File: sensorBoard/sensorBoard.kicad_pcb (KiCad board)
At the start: 4 copper layers, 204 x 100 mm, 162 parts, among them J10 Conn_01x07, J11 Conn_01x03, J12 Conn_01x02, J13 Conn_01x04, J14 Conn_01x05, J15 Conn_01x02, J16 Conn_01x02, J17 Conn_01x04, J18 Conn_01x07, J19 Conn_01x03, J20 Conn_01x02, J21 Conn_01x04, J22 Conn_01x05, J23 Conn_01x02, J24 Conn_01x02, J9 Conn_01x04, K5 G2RL-1-H, K6 G2RL-1-H, Q10 2N7002, Q11 2SC4213, Q12 NTD3055, Q19 2SC4213, Q2 2N7002, Q20 NTD3055, Q21 2N7002, Q22 2N7002, Q23 BSC440N10NS3G, Q24 BSC440N10NS3G, Q25 BSC440N10NS3G, Q26 BSC440N10NS3G, U12 MCP2551-I-SN, U17 LD1117S33TR_SOT223, U20 BTS50080-1TEA, U21 LM75C, U23 STM32L476RGTx, U32 BTS50080-1TEA, U33 LM75C, U35 STM32L476RGTx, U36 4011, U38 4011, U39 4011, U40 4011, U42 4N25, U43 4N25, U7 LD1117S33TR_SOT223, U9 MCP2551-I-SN, Y2 8MHz, Y3 8MHz

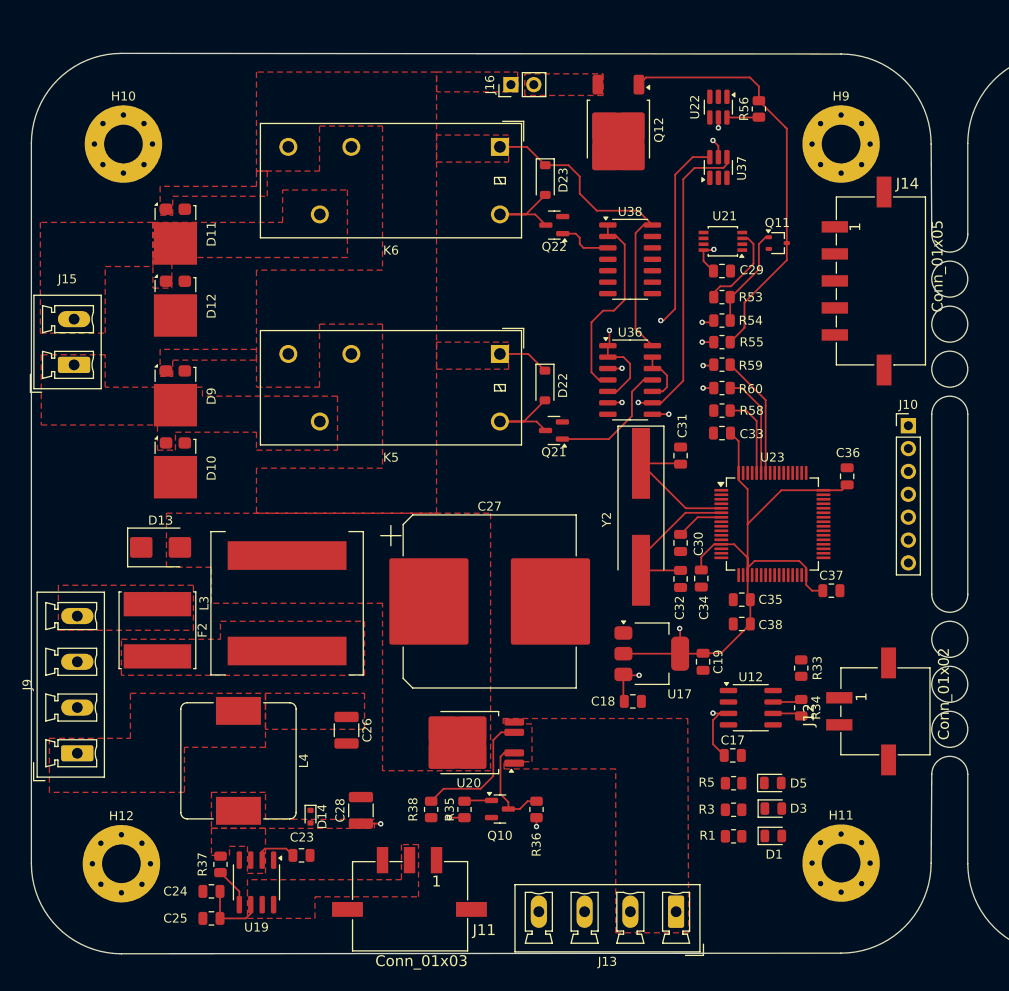
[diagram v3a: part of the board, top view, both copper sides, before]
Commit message: Das erstes PCB ist fast fertig. Die Vias waren auf die Platine platziert und Poligon war gefüllt.
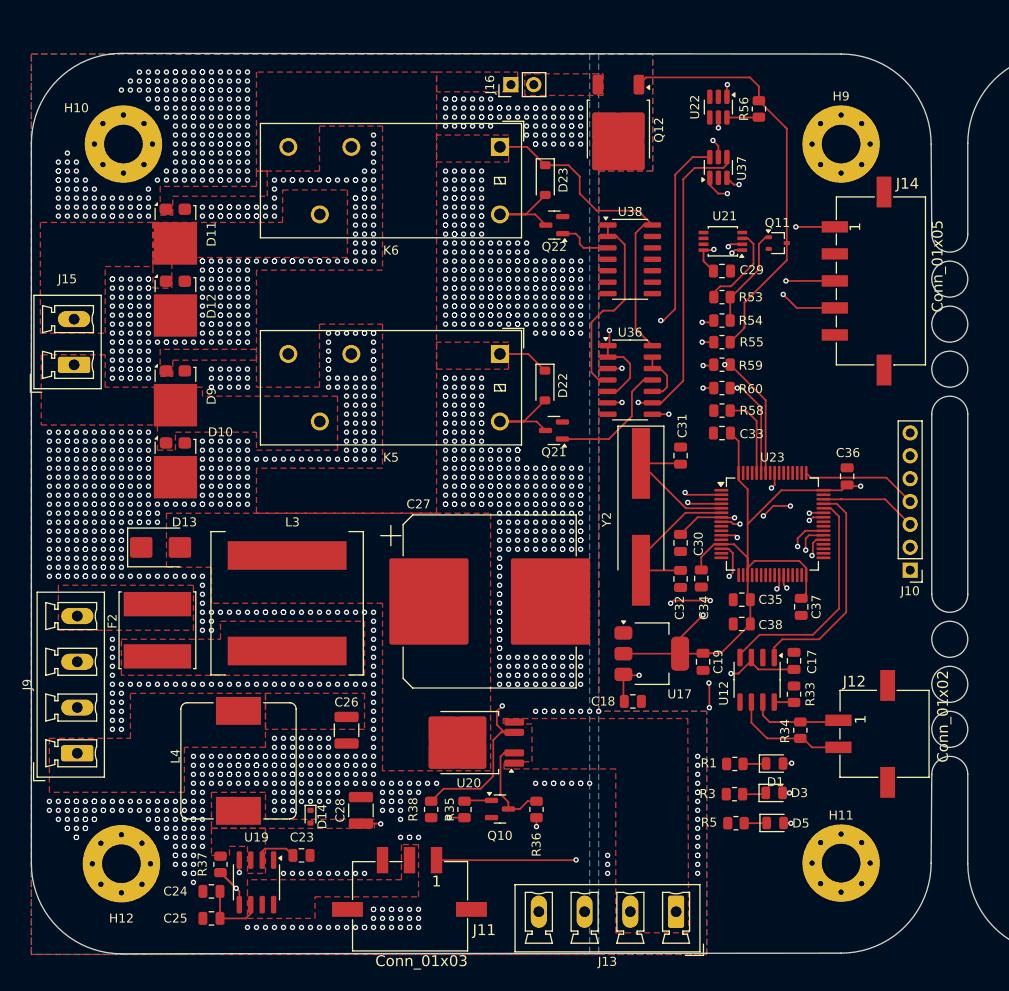
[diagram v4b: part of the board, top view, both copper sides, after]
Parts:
- moved J10 16.0 mm to (127.6, 97.3), turned to 180 degrees
- moved C17 12.5 mm to (114.7, 107.4), turned to 90 degrees
- moved D1 8.04 mm to (112.5, 118.8)
- moved R1 8.04 mm to (108.1, 118.8)
- moved D5 4.45 mm to (112.6, 125.4)
- moved R5 4.45 mm to (108.3, 125.4)
- moved C37 3.80 mm to (115.5, 101.4), turned to -90 degrees
- moved U12 3.18 mm to (110.6, 109.5), turned to -90 degrees
- moved R33 3.01 mm to (114.7, 111.1)
- moved J12 2.50 mm to (125.1, 115.5)
- moved R34 2.50 mm to (115.4, 115.1)
- moved R3 1.74 mm to (108.1, 122.2)
- moved D3 1.74 mm to (112.5, 122.1)
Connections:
- J10 pad 1: /Platine1/microcontroller1/UART_RX -> /Platine1/microcontroller1/UART_TX
- J10 pad 2: /Platine1/microcontroller1/UART_TX -> /Platine1/microcontroller1/UART_RX
- U23 pad 16: /Platine1/microcontroller1/UART_TX -> unconnected-(U23-PA2-Pad16)
- U23 pad 17: /Platine1/microcontroller1/UART_RX -> unconnected-(U23-PA3-Pad17)
- U23 pad 42: unconnected-(U23-PA9-Pad42) -> /Platine1/microcontroller1/UART_TX
- U23 pad 43: unconnected-(U23-PA10-Pad43) -> /Platine1/microcontroller1/UART_RX
- U35 pad 16: /Platine2/microcontroller2/UART_TX -> unconnected-(U35-PA2-Pad16)
- U35 pad 17: /Platine2/microcontroller2/UART_RX -> unconnected-(U35-PA3-Pad17)
- U35 pad 42: unconnected-(U35-PA9-Pad42) -> /Platine2/microcontroller2/UART_TX
- U35 pad 43: unconnected-(U35-PA10-Pad43) -> /Platine2/microcontroller2/UART_RX
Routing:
- net /Platine1/Commutation1-1/OVER_CURR_SERVO: track 4.43 -> 109.8 mm, vias 0 -> 2
- net /Platine1/Commutation1-1/SERVO_EN: track 0.00 -> 83.7 mm, vias 0 -> 4
- net /Platine1/SERVO_PWM: track 0.00 -> 59.8 mm, vias 0 -> 2
- net /Platine1/LED_EN: track 1.71 -> 58.9 mm, vias 1 -> 2
- net /Platine1/DIN: track 0.00 -> 56.5 mm, vias 0 -> 2
- net /Platine1/EN_MOTOR: track 0.00 -> 55.1 mm, vias 0 -> 2
- net /Platine1/TemperaturRegelung1/FAN_EN: track 0.00 -> 52.7 mm, vias 0 -> 2
- net /Platine1/IS_DIAG: track 14.7 -> 60.8 mm, vias 0 -> 4
- net Net-(D5-A): track 0.00 -> 34.3 mm, vias 0 -> 2
- net Net-(D3-A): track 0.00 -> 31.9 mm, vias 0 -> 2
- net /Platine1/I2C_SDA: track 11.6 -> 42.1 mm, vias 0 -> 3
- net Net-(D1-A): track 0.00 -> 29.4 mm, vias 0 -> 2
- net /Platine1/I2C_SCL: track 13.7 -> 42.6 mm, vias 0 -> 3
- net /Platine1/CanTransceiver1/CAN_RX: track 0.00 -> 25.8 mm
- net +3.3V: track 142.6 -> 167.9 mm, vias 7 -> 9
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- added copper zone on B.Cu, net GND
- added copper zone on F.Cu, net GND
- added copper zone on In1.Cu, net GND

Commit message: das erstes PCB ist fertig. Lightsensor check.
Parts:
- moved D20 224.7 mm to (372.6, 161.4)
- moved C44 224.7 mm to (357.1, 179.3)
- moved L5 224.7 mm to (389.3, 154.0)
- moved C43 224.7 mm to (380.4, 166.4)
- moved C45 224.7 mm to (380.4, 173.7)
- moved D21 224.7 mm to (373.9, 171.8)
- moved F3 224.7 mm to (373.4, 152.3)
- moved J17 224.7 mm to (359.9, 166.1)
- moved L6 224.7 mm to (391.9, 170.7)
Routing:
- net GND: track 0.00 -> 66.9 mm, vias 1865 -> 1879
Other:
- board text added: "12V"
- board text added: "3.3"
- board text added: "3.3V"
- board text added: "5V"
- board text added: "CAN_H"
- board text added: "CAN_L"
- board text added: "GND"
- board text added: "LED_OUT"
- board text added: "POLE+"
- board text added: "POLE-"
- board text added: "RST"
- board text added: "SCL"
- board text added: "SDA"
- board text added: "SWCLK"
- board text added: "SWDIO"
- board text added: "UART RX"
- board text added: "UART TX"

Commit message: Die zweite Leiterplatte ist fast fertig.
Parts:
- moved D19 269.9 mm to (147.0, 60.0), turned to 180 degrees
- moved J24 267.7 mm to (166.5, 48.0), turned to 90 degrees
- moved D18 262.0 mm to (147.0, 69.0), turned to 180 degrees
- moved Q20 261.1 mm to (176.0, 53.0), turned to -90 degrees
- moved C41 255.6 mm to (153.1, 137.0), turned to 180 degrees
- moved C42 255.3 mm to (153.1, 134.6), turned to 180 degrees
- moved D17 253.1 mm to (147.0, 88.3)
- moved U34 249.9 mm to (186.4, 76.0), turned to 90 degrees
- moved R23 249.8 mm to (154.0, 130.9), turned to -90 degrees
- moved D8 248.0 mm to (147.0, 78.6)
- moved U33 247.8 mm to (188.4, 86.0), turned to 180 degrees
- moved C46 246.0 mm to (190.2, 76.0), turned to -90 degrees
- moved Q19 245.3 mm to (185.6, 82.0)
- moved H7 245.2 mm to (144.0, 129.9)
- moved R44 245.1 mm to (181.2, 76.1), turned to -90 degrees
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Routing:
- net +5V: track 142.9 -> 307.2 mm, vias 5 -> 10
- net +3.3V: track 167.9 -> 327.2 mm, vias 9 -> 13
- net /Platine2/Commutation2-2/OVER_CURR_SERVO: track 0.00 -> 109.4 mm, vias 0 -> 4
- net /Platine2/Commutation2-2/SERVO_EN: track 0.00 -> 96.8 mm, vias 0 -> 2
- net /Platine2/I2C_SCL: track 0.00 -> 77.4 mm, vias 0 -> 2
- net /Platine2/I2C_SDA: track 0.00 -> 71.3 mm, vias 0 -> 2
- net /Platine2/SERVO_PWM: track 0.00 -> 67.7 mm, vias 0 -> 2
- net /Platine2/IS_DIAG: track 0.00 -> 64.8 mm, vias 0 -> 5
- net GND: track 66.9 -> 128.2 mm, vias 1879 -> 1997
- net Net-(U41-2Y): track 0.00 -> 59.9 mm, vias 0 -> 5
- net /Platine2/LED_EN: track 0.00 -> 59.4 mm, vias 0 -> 4
- net +12V: track 42.9 -> 101.7 mm, vias 0 -> 5
- net Net-(Q26-G): track 0.00 -> 50.1 mm, vias 0 -> 2
- net Net-(U41-1Y): track 0.00 -> 48.2 mm, vias 0 -> 2
- net Net-(Q24-G): track 0.00 -> 47.2 mm, vias 0 -> 2
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- added copper zone on F.Cu, net /Platine2/Commutation2-2/LAMP_OUT
- added copper zone on F.Cu, net /Platine2/Commutation2-2/POLE+
- added copper zone on F.Cu, net /Platine2/Commutation2-2/POLE-
- added copper zone on F.Cu, net /Platine2/Commutation2-2/SERVO_OUT
- added copper zone on F.Cu, net /Platine2/Protection2/12V_IN
- added copper zone on F.Cu, net /Platine2/Protection2/5V_IN
- added copper zone on F.Cu, net Net-(F3-Pad2)
- added copper zone on F.Cu, net Net-(J24-Pin_2)
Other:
- board size 204 x 100 mm -> 203.9 x 100 mm
- board text added: "RX"
- board text added: "TX"
- board text removed: "UART RX"
- board text removed: "UART TX"

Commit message: logo fällt
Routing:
- net GND: track 128.2 -> 140.5 mm, vias 1997 -> 4038
- net +3.3V: track 327.2 -> 330.3 mm
- net /Platine2/IS_DIAG: track 64.8 -> 66.4 mm
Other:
- board text added: "+"
- board text added: "-"
- board text added: "H"
- board text added: "L"
- board text removed: "CAN_H"
- board text removed: "CAN_L"
- board text removed: "POLE+"
- board text removed: "POLE-"

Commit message: logo und Signature wurden hinzufügt
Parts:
- added G***: LOGO, Kicad:paltech25_25, B.Cu at (57.6, 129.6)
- added G***: LOGO, Kicad:paltech25_25, B.Cu at (161.8, 128.7)
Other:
- board text added: "P.G."
